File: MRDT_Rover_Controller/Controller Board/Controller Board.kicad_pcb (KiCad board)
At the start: 2 copper layers, 137.6 x 81.5 mm, 18 parts, among them Q1 S8050, U1 MCP3008

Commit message: Added Pull-Up Resistors to ADC
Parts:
- added R7: 1K, Resistor_SMD:R_0603_1608Metric_Pad1.05x0.95mm_HandSolder, F.Cu at (169.3, 138.8)
- added R8: 1K, Resistor_SMD:R_0603_1608Metric_Pad1.05x0.95mm_HandSolder, F.Cu at (169.3, 141.3)
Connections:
- 16x2_LCD1 pad 2: Net-(16x2_LCD1-Pad2) -> +5V
- U1 pad 5: LeftSelect -> LFT_SEL
- U1 pad 6: RightSelect -> RGHT_SEL

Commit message: Updated Layout of PCB
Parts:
- moved C1 95.7 mm to (203.6, 55.4), turned to 180 degrees
- moved U1 93.0 mm to (106.0, 94.0)
- moved R5 91.0 mm to (83.8, 65.0), turned to 90 degrees
- moved R6 88.9 mm to (91.4, 65.0), turned to 90 degrees
- moved Left_Joystick1 79.3 mm to (90.2, 87.4)
- moved Right_Joystick1 77.7 mm to (199.4, 87.4)
- moved R2 76.4 mm to (131.6, 95.0)
- moved R3 76.3 mm to (131.6, 98.6), turned to 270 degrees
- moved I2C_Bus1 73.4 mm to (119.1, 94.0)
- moved R7 66.5 mm to (106.3, 117.3), turned to 180 degrees
- moved R8 65.8 mm to (106.4, 121.7), turned to 180 degrees
- moved JP1 65.3 mm to (98.3, 61.9), turned to 180 degrees
- moved 5V_Regulator1 62.3 mm to (207.0, 65.5), turned to 90 degrees
- moved ESP-12E1 59.6 mm to (142.9, 105.2), turned to 90 degrees
- moved R4 36.8 mm to (116.8, 119.1)
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
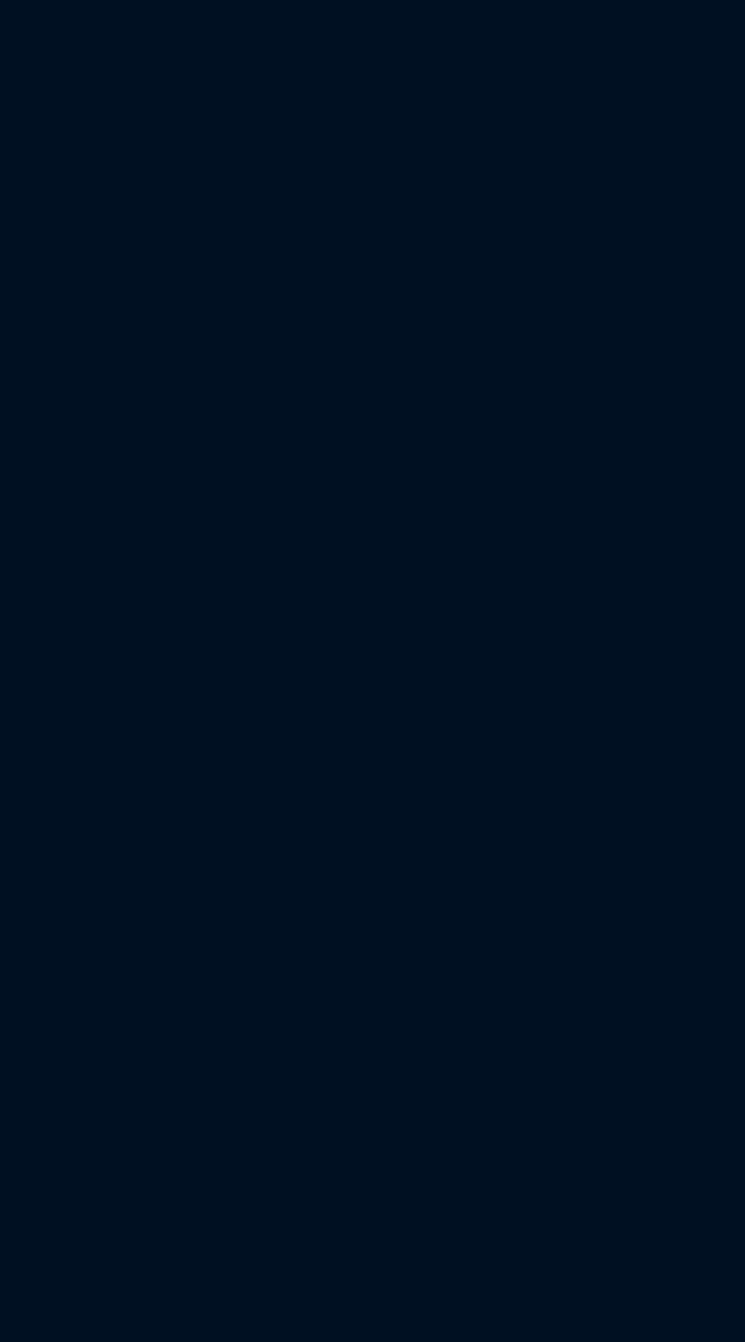
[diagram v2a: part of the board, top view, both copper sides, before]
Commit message: 9v Battery Holder Added
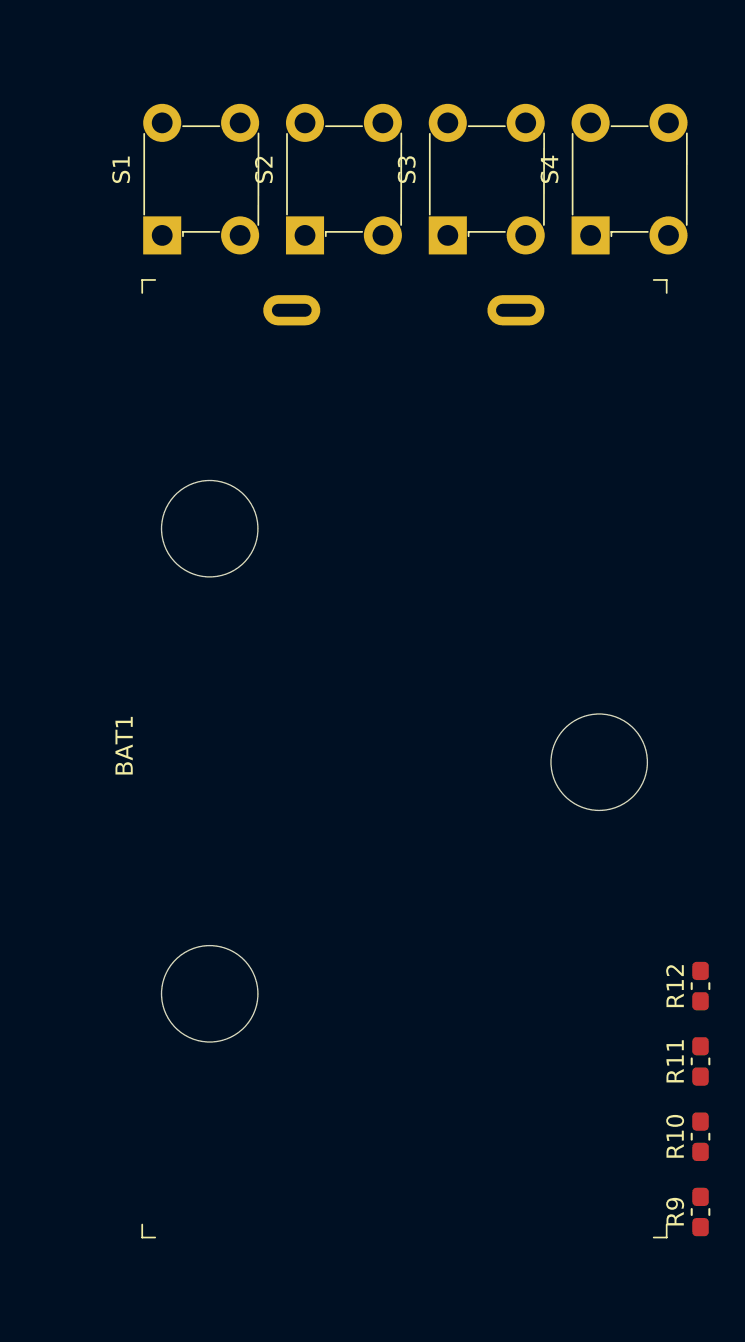
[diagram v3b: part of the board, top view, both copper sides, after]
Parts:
- added BAT1: BC9VPC, digikey-footprints:Battery_Holder_9V_BC9VPC-ND, F.Cu at (242.6, 85.3)
- added R10: 100, Resistor_SMD:R_0603_1608Metric_Pad1.05x0.95mm_HandSolder, F.Cu at (270.9, 120.5)
- added R11: 100, Resistor_SMD:R_0603_1608Metric_Pad1.05x0.95mm_HandSolder, F.Cu at (270.9, 116.1)
- added R12: 100, Resistor_SMD:R_0603_1608Metric_Pad1.05x0.95mm_HandSolder, F.Cu at (270.9, 111.8)
- added R9: 100, Resistor_SMD:R_0603_1608Metric_Pad1.05x0.95mm_HandSolder, F.Cu at (270.9, 124.8)
- added S1: 1825910-6, digikey-footprints:Switch_Tactile_THT_6x6mm, F.Cu at (239.8, 68.4)
- added S2: 1825910-6, digikey-footprints:Switch_Tactile_THT_6x6mm, F.Cu at (248.1, 68.4)
- added S3: 1825910-6, digikey-footprints:Switch_Tactile_THT_6x6mm, F.Cu at (256.3, 68.4)
- added S4: 1825910-6, digikey-footprints:Switch_Tactile_THT_6x6mm, F.Cu at (264.6, 68.4)
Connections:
- ESP-12E1 pad 11: Net-(ESP-12E1-Pad11) -> SW3
- ESP-12E1 pad 13: Net-(ESP-12E1-Pad13) -> SW4
- ESP-12E1 pad 7: Net-(ESP-12E1-Pad7) -> SW1
- ESP-12E1 pad 9: Net-(ESP-12E1-Pad9) -> SW2

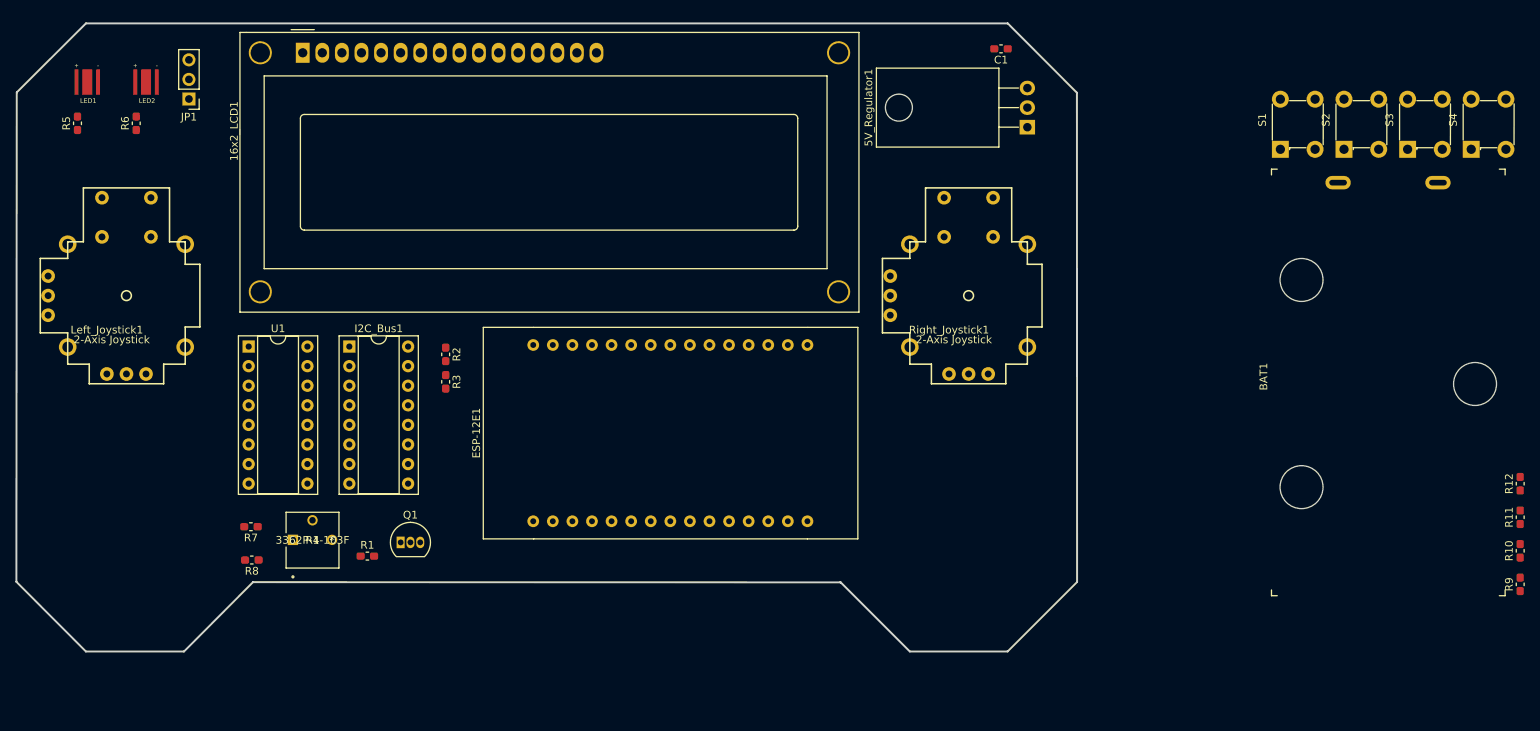
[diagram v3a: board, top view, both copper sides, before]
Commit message: Updated Net, and Started PCB Traces
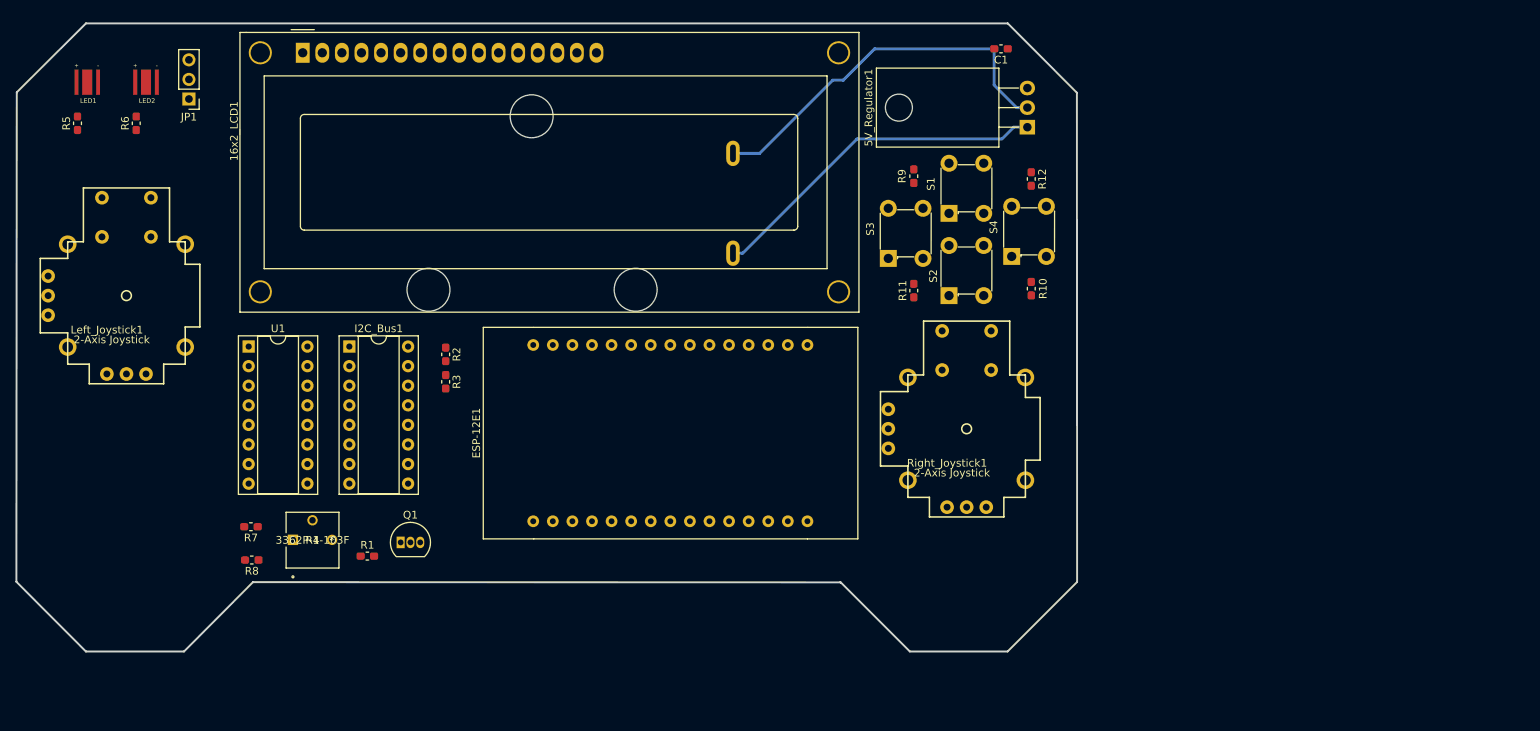
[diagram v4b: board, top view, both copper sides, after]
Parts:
- BAT1: moved to B.Cu
- moved R9 94.8 mm to (192.3, 71.9), turned to 270 degrees
- moved BAT1 86.4 mm to (156.2, 86.6), turned to 0 degrees
- moved R11 84.0 mm to (192.3, 86.7)
- moved R12 74.7 mm to (207.5, 72.2), turned to 270 degrees
- moved R10 71.9 mm to (207.5, 86.5)
- moved S3 68.8 mm to (189.0, 82.5)
- moved S4 61.2 mm to (205.0, 82.3)
- moved S2 54.6 mm to (196.8, 87.4)
- moved S1 43.8 mm to (196.8, 76.7)
- moved Right_Joystick1 17.3 mm to (199.1, 104.6)
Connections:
- net +5V renamed 5V
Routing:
- net GNDREF: track 0.00 -> 49.2 mm
- net Net-(5V_Regulator1-Pad1): track 0.00 -> 44.9 mm

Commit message: PCB Traces Updated
Traces connected to right joystick and pushbuttons
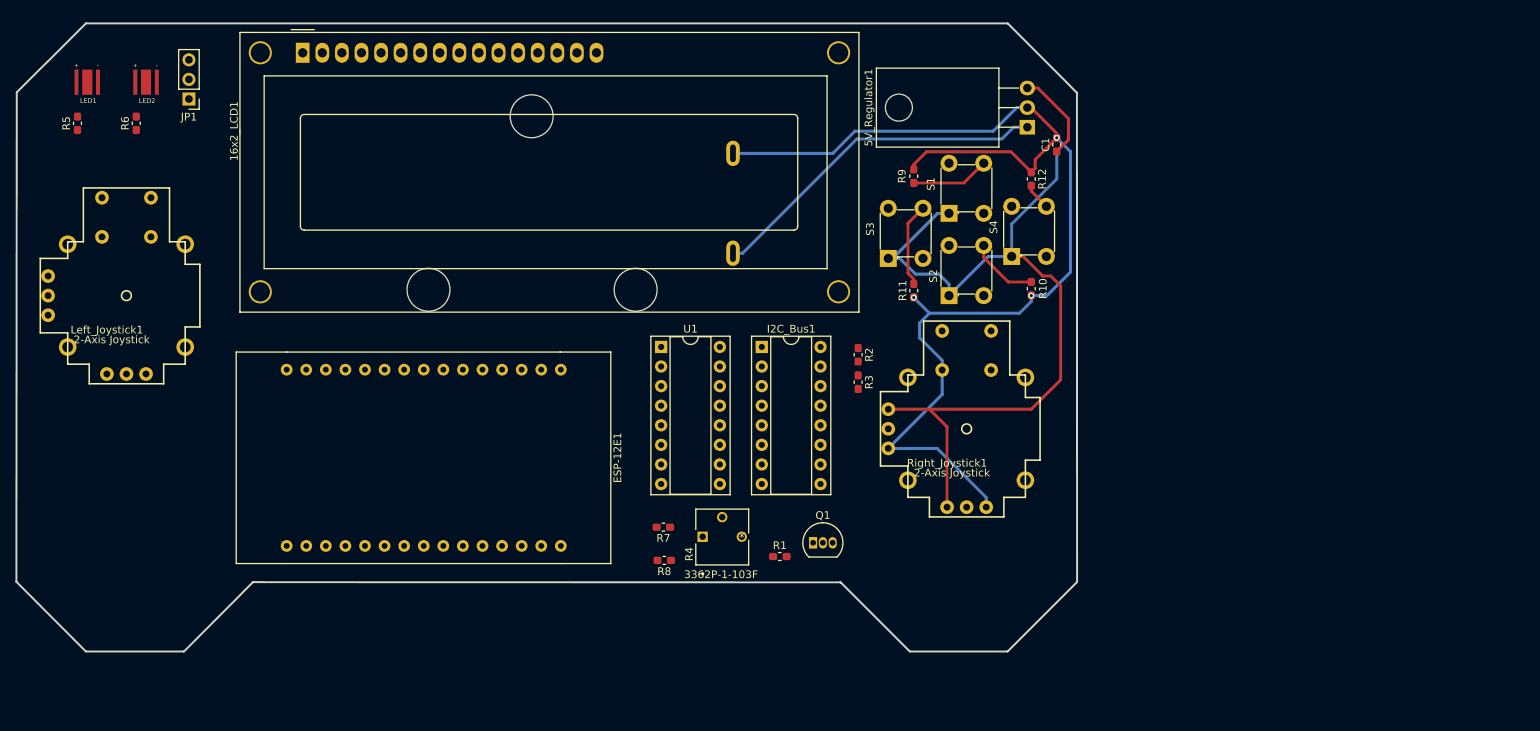
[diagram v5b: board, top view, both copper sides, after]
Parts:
- moved I2C_Bus1 53.5 mm to (172.6, 94.0)
- moved R1 53.5 mm to (174.9, 121.2)
- moved R2 53.5 mm to (185.1, 95.0)
- moved R3 53.5 mm to (185.1, 98.6)
- moved U1 53.5 mm to (159.5, 94.0)
- moved Q1 53.5 mm to (179.2, 119.4)
- moved R7 53.5 mm to (159.8, 117.4)
- moved R8 53.5 mm to (159.9, 121.7)
- moved R4 53.1 mm to (170.0, 118.7)
- moved C1 14.4 mm to (210.8, 67.8), turned to 90 degrees
- moved ESP-12E1 4.80 mm to (146.5, 108.4), turned to 270 degrees
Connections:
- 5V_Regulator1 pad 2: GNDREF -> GND
- BAT1 pad NEG: GNDREF -> GND
- C1 pad 2: GNDREF -> GND
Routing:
- net GND: track 0.00 -> 150.6 mm, vias 0 -> 3
- net 5V: track 0.00 -> 116.7 mm
- net GNDREF: track 49.2 -> 0.00 mm
- net SW3: track 0.00 -> 10.9 mm
- net SW1: track 0.00 -> 10.1 mm
- net SW2: track 0.00 -> 9.04 mm
- net SW4: track 0.00 -> 3.48 mm

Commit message: Trace Update
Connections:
- Left_Joystick1 pad B1A: LeftSelect -> LFT_SEL
- Right_Joystick1 pad B1A: RightSelect -> RGHT_SEL
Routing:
- net GND: track 150.6 -> 225.5 mm
- net 5V: track 116.7 -> 164.4 mm
- net SDA: track 0.00 -> 5.15 mm
- net SCL: track 0.00 -> 5.03 mm
